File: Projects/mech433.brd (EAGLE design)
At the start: 100 x 100 mm, 23 parts, among them J1 USB-MB-H

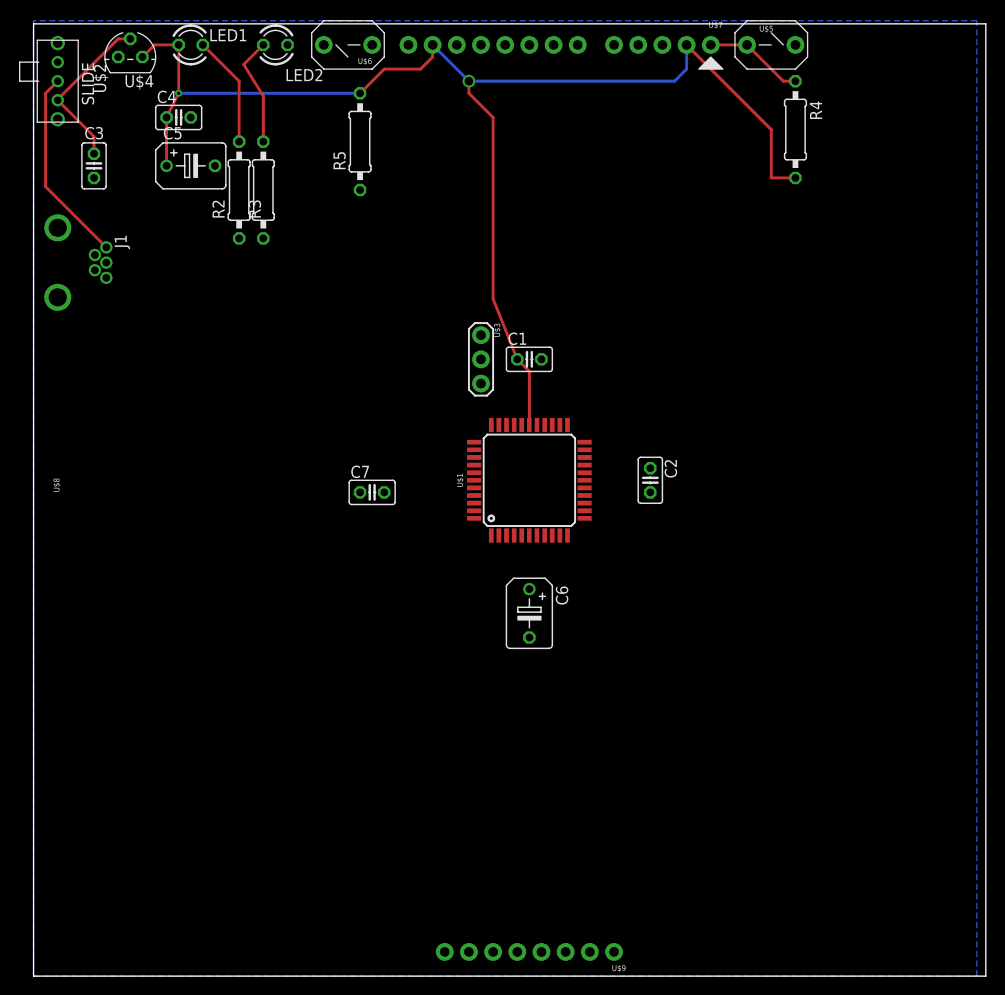
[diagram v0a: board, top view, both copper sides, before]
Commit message: Connected 3.3 Volts
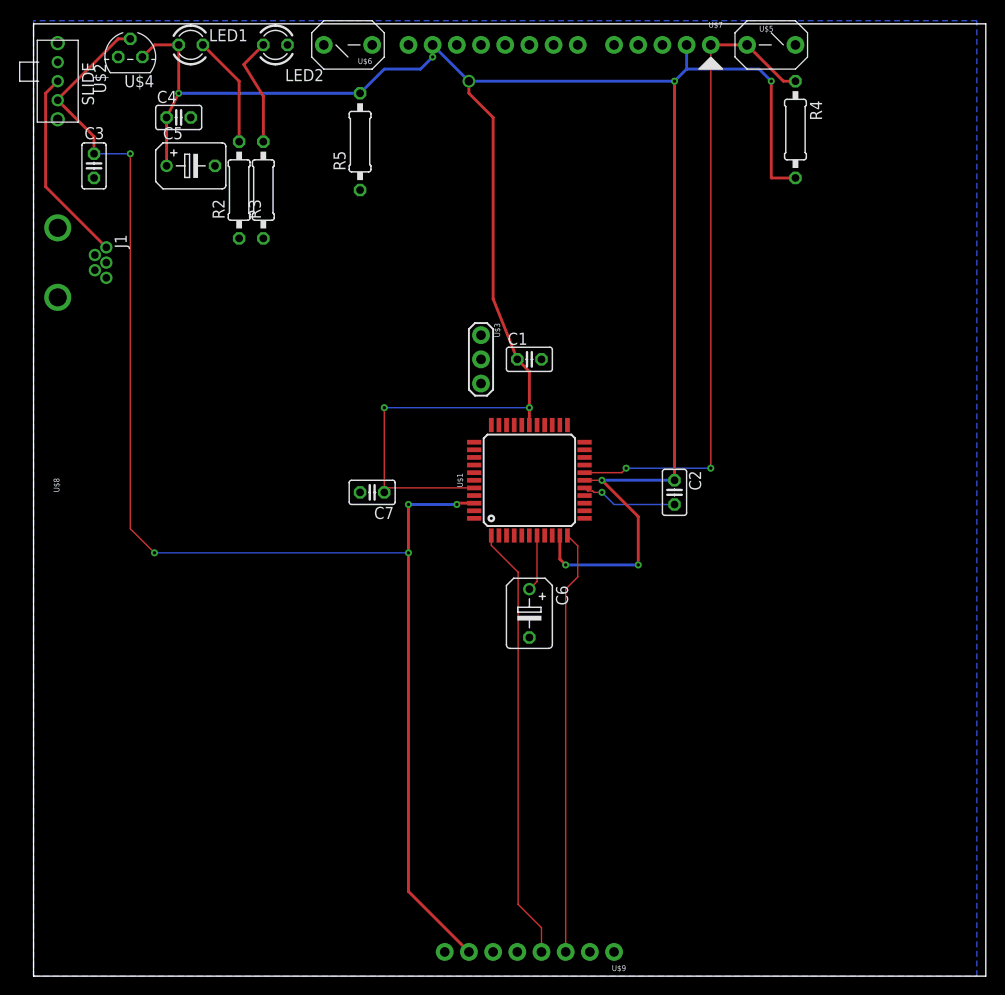
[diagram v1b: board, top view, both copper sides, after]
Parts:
- moved C2 2.84 mm to (67.3, 50.8)
- turned C7 to 180 degrees
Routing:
- net +5V: track 17.7 -> 147.7 mm, vias 0 -> 5
- net +3V3: track 136.5 -> 245.0 mm, vias 2 -> 10
- net MCLR: track 10.5 -> 68.4 mm, vias 0 -> 2
- net B9: track 0.00 -> 45.9 mm
- net B13: track 0.00 -> 44.7 mm
- net GND: track 0.00 -> 10.2 mm, vias 0 -> 1
- net N$6: track 0.00 -> 5.96 mm

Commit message: Connected All of the Power and GND
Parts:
- moved C1 1.27 mm to (52.1, 66.0)
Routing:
- net A4: track 0.00 -> 73.7 mm, vias 0 -> 2
- net B4: track 0.00 -> 67.1 mm, vias 0 -> 6
- net GND: track 10.2 -> 45.0 mm, vias 1 -> 3
- net N$4: track 0.00 -> 10.9 mm
- net +3V3: track 245.0 -> 254.5 mm, vias 10 -> 9
- net N$5: track 0.00 -> 5.47 mm

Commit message: Completed_all_basic_connections
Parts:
- moved C1 1.80 mm to (50.8, 67.3)
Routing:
- net D-: track 0.00 -> 86.3 mm, vias 0 -> 2
- net D+: track 0.00 -> 78.0 mm, vias 0 -> 3
- net USBID: track 0.00 -> 67.5 mm, vias 0 -> 2
- net A0: track 0.00 -> 59.1 mm, vias 0 -> 2
- net A1: track 0.00 -> 57.5 mm, vias 0 -> 2
- net B7: track 0.00 -> 54.8 mm
- net B8: track 0.00 -> 53.8 mm
- net B15: track 0.00 -> 50.5 mm
- net B14: track 0.00 -> 49.4 mm
- net PGD1: track 0.00 -> 47.0 mm
- net PGC1: track 0.00 -> 44.5 mm
- net B3: track 0.00 -> 42.3 mm
- net B2: track 0.00 -> 41.6 mm
- net +5V: track 147.7 -> 155.3 mm
- net GND: track 45.0 -> 49.5 mm, vias 3 -> 2
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
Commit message: Error_Checked
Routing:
- net GND: track 49.5 -> 47.7 mm
- net A1: track 57.5 -> 58.2 mm
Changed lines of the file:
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@@
 <layers>
 <layer number="1" name="Top" color="4" fill="1" visible="yes" active="yes"/>
+<layer number="2" name="Route2" color="16" fill="1" visible="no" active="yes"/>
+<layer number="3" name="Route3" color="17" fill="1" visible="no" active="yes"/>
+<layer number="4" name="Route4" color="18" fill="1" visible="no" active="yes"/>
+<layer number="5" name="Route5" color="19" fill="1" visible="no" active="yes"/>
+<layer number="6" name="Route6" color="25" fill="1" visible="no" active="yes"/>
+<layer number="7" name="Route7" color="26" fill="1" visible="no" active="yes"/>
+<layer number="8" name="Route8" color="27" fill="1" visible="no" active="yes"/>
+<layer number="9" name="Route9" color="28" fill="1" visible="no" active="yes"/>
+<layer number="10" name="Route10" color="29" fill="1" visible="no" active="yes"/>
+<layer number="11" name="Route11" color="30" fill="1" visible="no" active="yes"/>
+<layer number="12" name="Route12" color="20" fill="1" visible="no" active="yes"/>
+<layer number="13" name="Route13" color="21" fill="1" visible="no" active="yes"/>
+<layer number="14" name="Route14" color="22" fill="1" visible="no" active="yes"/>
+<layer number="15" name="Route15" color="23" fill="1" visible="no" active="yes"/>
 <layer number="16" name="Bottom" color="1" fill="1" visible="yes" active="yes"/>
 <layer number="17" name="Pads" color="2" fill="1" visible="yes" active="yes"/>
@@
 </class>
 </classes>
-<designrules name="default">
+<designrules name="SeeedStudio_2layer_DRU_no_angle_20140221">
 <description language="de">&lt;b&gt;EAGLE Design Rules&lt;/b&gt;
 &lt;p&gt;
@@
 necessary adjustments and save your customized
 design rules under a new name.</description>
+<description language="zh">&lt;b&gt;Seeed Studio EAGLE Design Rules&lt;/b&gt;
+</description>
 <param name="layerSetup" value="(1*16)"/>
-<param name="mtCopper" value="0.035mm 0.035mm 0.035mm 0.035mm 0.035mm 0.035mm 0.035mm 0.035mm 0.035mm 0.035mm 0.035mm 0.035mm 0.035mm 0.035mm 0.035mm 0.035mm"/>
-<param name="mtIsolate" value="1.5mm 0.15mm 0.2mm 0.15mm 0.2mm 0.15mm 0.2mm 0.15mm 0.2mm 0.15mm 0.2mm 0.15mm 0.2mm 0.15mm 0.2mm"/>
+<param name="mtCopper" value="0.035mm 0.0175mm 0.035mm 0.035mm 0.035mm 0.035mm 0.035mm 0.035mm 0.035mm 0.035mm 0.035mm 0.035mm 0.035mm 0.035mm 0.0175mm 0.035mm"/>
+<param name="mtIsolate" value="1.5mm 1.1mm 0.2mm 0.15mm 0.2mm 0.15mm 0.2mm 0.15mm 0.2mm 0.15mm 0.2mm 0.15mm 0.2mm 0.15mm 0.2mm"/>
 <param name="mdWireWire" value="6mil"/>
 <param name="mdWirePad" value="6mil"/>
@@
 <param name="mdPadVia" value="6mil"/>
 <param name="mdViaVia" value="6mil"/>
-<param name="mdSmdPad" value="6mil"/>
-<param name="mdSmdVia" value="6mil"/>
-<param name="mdSmdSmd" value="6mil"/>
-<param name="mdViaViaSameLayer" value="6mil"/>
+<param name="mdSmdPad" value="0mil"/>
+<param name="mdSmdVia" value="0mil"/>
+<param name="mdSmdSmd" value="0mil"/>
+<param name="mdViaViaSameLayer" value="8mil"/>
 <param name="mnLayersViaInSmd" value="2"/>
-<param name="mdCopperDimension" value="40mil"/>
-<param name="mdDrill" value="6mil"/>
+<param name="mdCopperDimension" value="10mil"/>
+<param name="mdDrill" value="10mil"/>
 <param name="mdSmdStop" value="0mil"/>
 <param name="msWidth" value="6mil"/>
-<param name="msDrill" value="0.35mm"/>
-<param name="msMicroVia" value="9.99mm"/>
+<param name="msDrill" value="12mil"/>
+<param name="msMicroVia" value="12mil"/>
 <param name="msBlindViaRatio" value="0.5"/>
 <param name="rvPadTop" value="0.25"/>
@@
 <param name="rlMinPadBottom" value="10mil"/>
 <param name="rlMaxPadBottom" value="20mil"/>
-<param name="rlMinViaOuter" value="8mil"/>
+<param name="rlMinViaOuter" value="6mil"/>
 <param name="rlMaxViaOuter" value="20mil"/>
-<param name="rlMinViaInner" value="8mil"/>
+<param name="rlMinViaInner" value="6mil"/>
 <param name="rlMaxViaInner" value="20mil"/>
 <param name="rlMinMicroViaOuter" value="4mil"/>
@@
 <param name="psTop" value="-1"/>
 <param name="psBottom" value="-1"/>
-<param name="psFirst" value="-1"/>
+<param name="psFirst" value="0"/>
 <param name="psElongationLong" value="100"/>
 <param name="psElongationOffset" value="100"/>
 <param name="mvStopFrame" value="1"/>
 <param name="mvCreamFrame" value="0"/>
-<param name="mlMinStopFrame" value="4mil"/>
-<param name="mlMaxStopFrame" value="4mil"/>
+<param name="mlMinStopFrame" value="2mil"/>
+<param name="mlMaxStopFrame" value="2mil"/>
 <param name="mlMinCreamFrame" value="0mil"/>
 <param name="mlMaxCreamFrame" value="0mil"/>
-<param name="mlViaStopLimit" value="0mil"/>
+<param name="mlViaStopLimit" value="100mil"/>
 <param name="srRoundness" value="0"/>
 <param name="srMinRoundness" value="0mil"/>
@@
 <param name="checkAngle" value="0"/>
 <param name="checkFont" value="1"/>
-<param name="checkRestrict" value="1"/>
+<param name="checkRestrict" value="0"/>
 <param name="checkStop" value="0"/>
 <param name="checkValues" value="0"/>
@@
 </polygon>
 <wire x1="67.31" y1="49.53" x2="60.96" y2="49.53" width="0.1524" layer="16"/>
-<wire x1="60.96" y1="49.53" x2="59.69" y2="50.8" width="0.1524" layer="16"/>
 <wire x1="52.07" y1="67.31" x2="52.07" y2="63.5" width="0.1524" layer="16"/>
 <wire x1="52.07" y1="63.5" x2="50.8" y2="62.23" width="0.1524" layer="16"/>
@@
 <via x="64.77" y="57.15" extent="1-16" drill="0.35"/>
 <wire x1="64.77" y1="57.15" x2="64.77" y2="54.61" width="0.1524" layer="1"/>
-<wire x1="64.77" y1="54.61" x2="58.42" y2="54.61" width="0.1524" layer="1"/>
-<wire x1="57.87" y1="54.47" x2="58.42" y2="54.61" width="0" layer="19" extent="1-1"/>
+<wire x1="64.77" y1="54.61" x2="64.77" y2="54.455190625" width="0.1524" layer="1"/>
+<wire x1="64.77" y1="54.61" x2="64.63" y2="54.47" width="0.1524" layer="1"/>
+<wire x1="64.63" y1="54.47" x2="57.87" y2="54.47" width="0.1524" layer="1"/>
 </signal>
 <signal name="B15">
@@
 <contactref element="U$9" pad="1"/>
 <wire x1="60.96" y1="2.54" x2="60.96" y2="49.53" width="0.1524" layer="1"/>
-<wire x1="60.96" y1="49.53" x2="60.06244375" y2="50.42755625" width="0.1524" layer="1"/>
-<wire x1="60.06244375" y1="50.42755625" x2="57.791475" y2="50.42755625" width="0.1524" layer="1"/>
-<wire x1="57.791475" y1="50.42755625" x2="57.87" y2="50.47" width="0" layer="19" extent="1-1"/>
+<wire x1="60.96" y1="49.53" x2="59.69" y2="50.8" width="0.1524" layer="1"/>
+<wire x1="59.69" y1="50.8" x2="58.7232875" y2="50.8" width="0.1524" layer="1"/>
+<wire x1="58.7232875" y1="50.8" x2="58.7146875" y2="50.7914" width="0.1524" layer="1"/>
+<wire x1="58.7146875" y1="50.7914" x2="58.1914" y2="50.7914" width="0.1524" layer="1"/>
+<wire x1="58.1914" y1="50.7914" x2="57.87" y2="50.47" width="0.1524" layer="1"/>
 </signal>
 <signal name="B14">
@@
 <contactref element="U$9" pad="5"/>
 <wire x1="50.8" y1="2.54" x2="41.401409375" y2="11.938590625" width="0.1524" layer="1"/>
-<wire x1="41.401409375" y1="11.938590625" x2="41.401409375" y2="47.20106875" width="0.1524" layer="1"/>
+<wire x1="41.401409375" y1="11.938590625" x2="41.401409375" y2="48.06711875" width="0.1524" layer="1"/>
 <wire x1="46.249265625" y1="48.090734375" x2="46.27" y2="48.07" width="0.1524" layer="1"/>
-<wire x1="41.401409375" y1="47.20106875" x2="42.28901875" y2="48.088678125" width="0.1524" layer="1"/>
-<wire x1="46.27" y1="48.07" x2="46.251321875" y2="48.088678125" width="0.1524" layer="1"/>
-<wire x1="46.251321875" y1="48.088678125" x2="42.28901875" y2="48.088678125" width="0.1524" layer="1"/>
+<wire x1="46.27" y1="48.07" x2="46.26711875" y2="48.06711875" width="0.1524" layer="1"/>
+<wire x1="46.26711875" y1="48.06711875" x2="41.401409375" y2="48.06711875" width="0.1524" layer="1"/>
 </signal>
 <signal name="A4">
@@
 <mfgpreviewcolor name="substratecolor" color="0xFF786E46"/>
 </mfgpreviewcolors>
+<errors>
+</errors>
 </board>
 </drawing>
